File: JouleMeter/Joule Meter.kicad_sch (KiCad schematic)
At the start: 65 parts, among them J1 XT60-M, J2 XT60-M, J3 22035035, J4 22035035, U1 LMR36510, U3 INA240A1PW, U4 ADS1118IDGS-Q1, U5 MCP6286T-E/OT1

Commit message: Complete Draft Layout
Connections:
- net GND: now also U1.9 (PAD)
- net CAN_H renamed CAN_P
- net CAN_L renamed CAN_N
- no-connect marks 2 -> 1
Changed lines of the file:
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@@
+	)
+	(junction
+		(at 104.14 85.09)
+		(diameter 0)
+		(color 0 0 0 0)
 	)
 	(junction
@@
 		(at 229.87 146.05)
 	)
-	(no_connect
-		(at 106.68 83.82)
-	)
 	(wire
 		(pts
@@
 	(wire
 		(pts
+			(xy 106.68 85.09) (xy 104.14 85.09)
+		)
+		(stroke
+			(width 0)
+			(type default)
+		)
+	)
+	(wire
+		(pts
 			(xy 200.66 55.88) (xy 200.66 58.42)
 		)
@@
 	(wire
 		(pts
+			(xy 104.14 85.09) (xy 104.14 86.36)
+		)
+		(stroke
+			(width 0)
+			(type default)
+		)
+	)
+	(wire
+		(pts
 			(xy 196.85 143.51) (xy 196.85 146.05)
 		)
@@
 	(wire
 		(pts
-			(xy 104.14 83.82) (xy 104.14 86.36)
+			(xy 104.14 83.82) (xy 104.14 85.09)
 		)
 		(stroke
@@
 		(pts
 			(xy 304.8 71.12) (xy 304.8 76.2)
+		)
+		(stroke
+			(width 0)
+			(type default)
+		)
+	)
+	(wire
+		(pts
+			(xy 106.68 83.82) (xy 106.68 85.09)
 		)
 		(stroke
@@
 		)
 	)
-	(label "CAN_L"
+	(label "CAN_N"
 		(at 285.75 200.66 180)
 		(effects
@@
 		)
 	)
-	(label "CAN_H"
+	(label "CAN_P"
 		(at 280.67 185.42 180)
 		(effects

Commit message: PCB Complete Draft
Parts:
- removed TP19: CT-RXD, TestPoint:TestPoint_Pad_1.0x1.0mm, symbol Connector:TestPoint
- removed TP20: CT-TXD, TestPoint:TestPoint_Pad_1.0x1.0mm, symbol Connector:TestPoint
- added J5: M22-7130442, SMV_Joule:HARWIN_M22-7130442, symbol Joule Meter:M22-7130442
- R0: footprint SMV_Joule:WSBS8518_VIS-L -> SMV_Joule:RESC10052X145N
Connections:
- net CAN-TXD: now also J5.1
- net CAN_RXD: now also J5.4
- net GND: now also J5.2, J5.3
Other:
- moved on the sheet: C21, C23, J3, J4, MCP2562, TP15, TP16

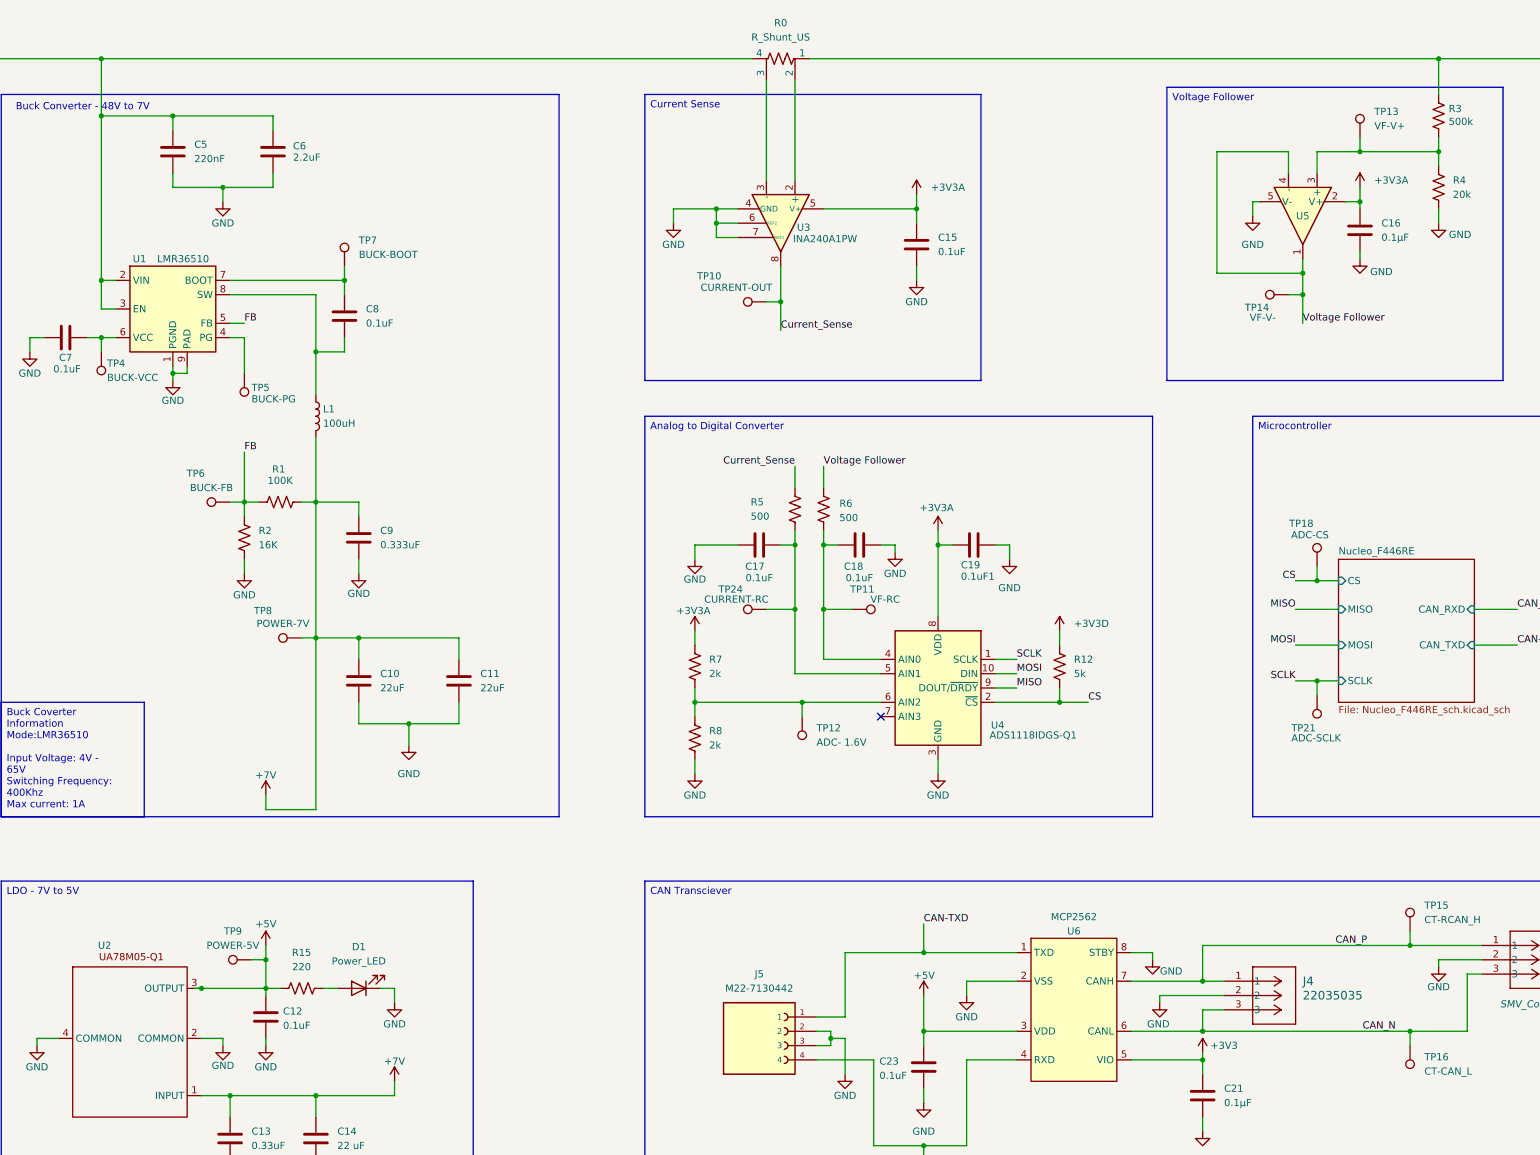
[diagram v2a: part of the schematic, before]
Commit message: Revised Version Part 1
Implemented changes from Google Docs and Dylan
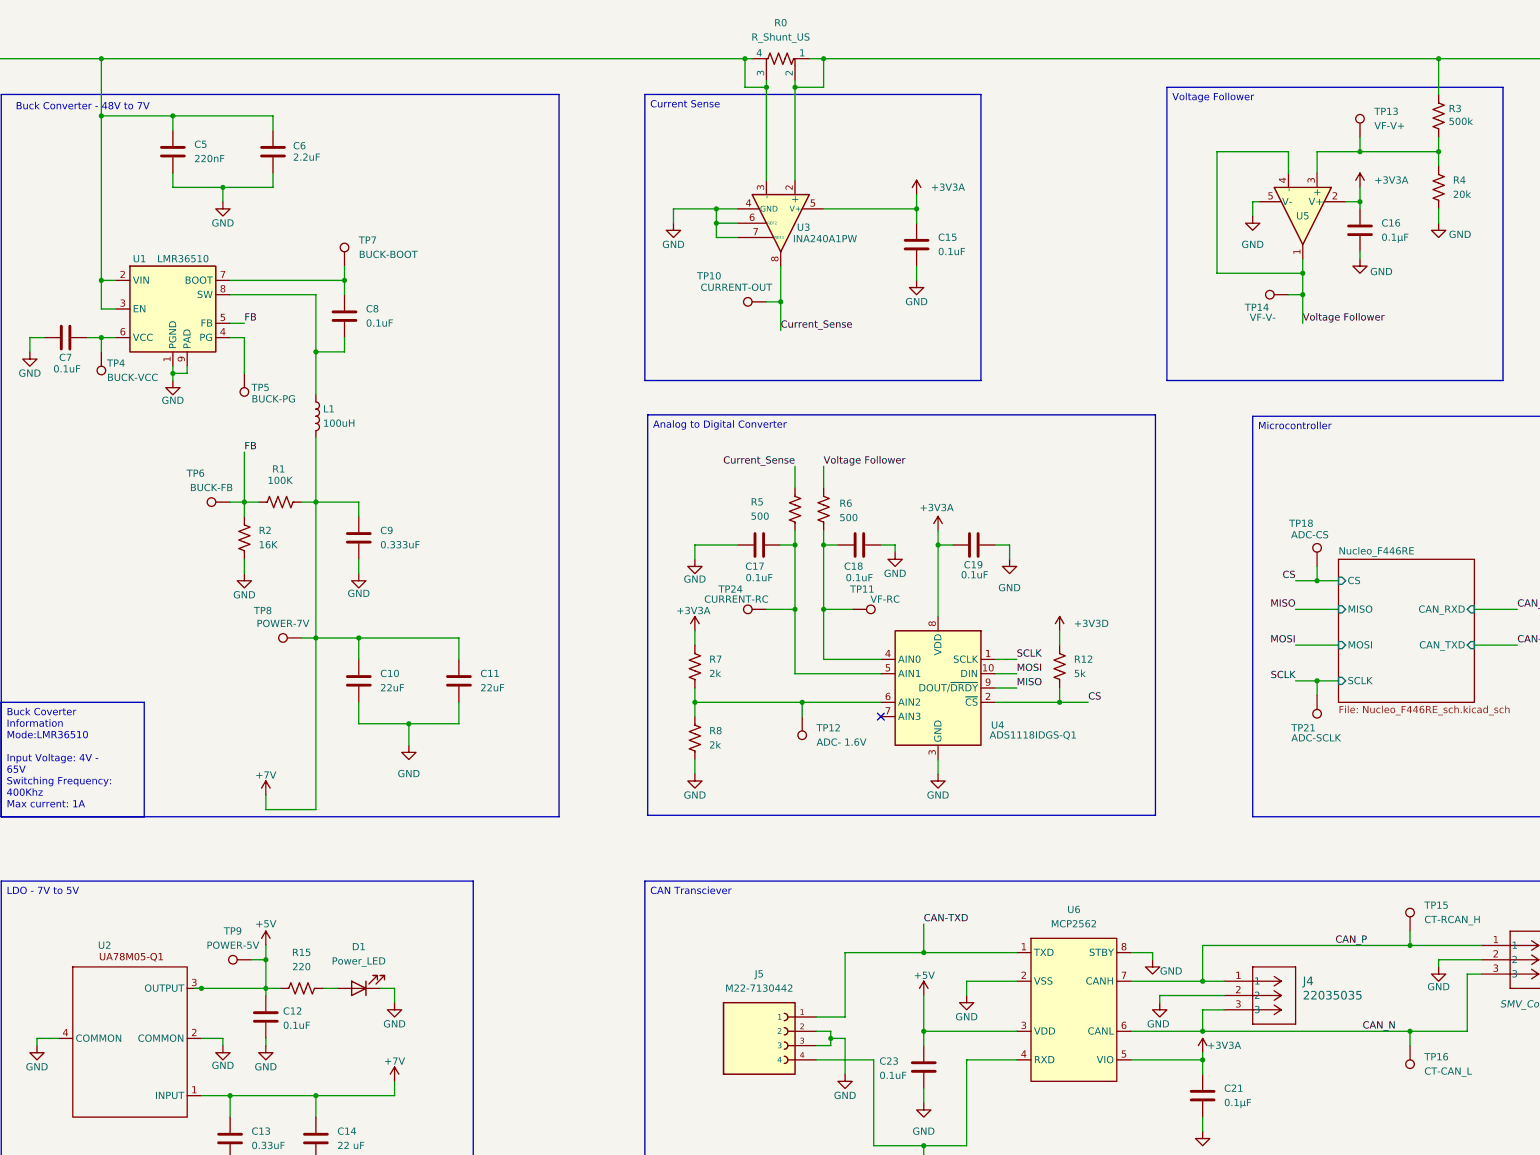
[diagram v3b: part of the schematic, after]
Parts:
- C19: renamed from 0.1uF1; value C19 -> 0.1uF
- U6: renamed from MCP2562; value U6 -> MCP2562
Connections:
- net +3V3 is gone; now on net +3V3A: C21.1, U6.5 (VIO)
- net at C1.2, C2.1, J1.P (POS)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: now also R0.2, U3.2 (+)
- net at R0.3, U3.3 (-): now also C3.2, C4.1, C5.2, C6.2, J2.P (POS), R0.4, TP3.1, U1.2 (VIN), U1.3 (EN)
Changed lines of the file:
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@@
 	(text_box "Analog to Digital Converter"
 		(exclude_from_sim no)
-		(at 187.96 92.71 0)
+		(at 188.468 92.456 0)
 		(size 90.17 71.12)
 		(margins 0.9525 0.9525 0.9525 0.9525)
@@
 	)
 	(junction
+		(at 209.55 34.29)
+		(diameter 0)
+		(color 0 0 0 0)
+	)
+	(junction
 		(at 328.93 45.72)
 		(diameter 0)
@@
 	)
 	(junction
+		(at 219.71 29.21)
+		(diameter 0)
+		(color 0 0 0 0)
+	)
+	(junction
 		(at 323.85 186.69)
 		(diameter 0)
@@
 	)
 	(junction
+		(at 214.63 34.29)
+		(diameter 0)
+		(color 0 0 0 0)
+	)
+	(junction
 		(at 129.54 107.95)
 		(diameter 0)
@@
 	)
 	(junction
+		(at 205.74 29.21)
+		(diameter 0)
+		(color 0 0 0 0)
+	)
+	(junction
 		(at 363.22 29.21)
 		(diameter 0)
@@
 	(wire
 		(pts
-			(xy 214.63 33.02) (xy 214.63 50.8)
+			(xy 214.63 33.02) (xy 214.63 34.29)
 		)
 		(stroke
@@
 	(wire
 		(pts
-			(xy 217.17 29.21) (xy 328.93 29.21)
+			(xy 217.17 29.21) (xy 219.71 29.21)
 		)
 		(stroke
@@
 	(wire
 		(pts
+			(xy 209.55 34.29) (xy 205.74 34.29)
+		)
+		(stroke
+			(width 0)
+			(type default)
+		)
+	)
+	(wire
+		(pts
 			(xy 196.85 115.57) (xy 204.47 115.57)
 		)
@@
 	(wire
 		(pts
+			(xy 205.74 34.29) (xy 205.74 29.21)
+		)
+		(stroke
+			(width 0)
+			(type default)
+		)
+	)
+	(wire
+		(pts
 			(xy 129.54 224.79) (xy 129.54 228.6)
 		)
@@
 	(wire
 		(pts
+			(xy 219.71 29.21) (xy 328.93 29.21)
+		)
+		(stroke
+			(width 0)
+			(type default)
+		)
+	)
+	(wire
+		(pts
 			(xy 287.02 201.93) (xy 323.85 201.93)
 		)
@@
 	(wire
 		(pts
+			(xy 214.63 34.29) (xy 214.63 50.8)
+		)
+		(stroke
+			(width 0)
+			(type default)
+		)
+	)
+	(wire
+		(pts
 			(xy 287.02 193.04) (xy 290.83 193.04)
 		)
@@
 	(wire
 		(pts
-			(xy 91.44 29.21) (xy 207.01 29.21)
+			(xy 91.44 29.21) (xy 205.74 29.21)
 		)
 		(stroke
@@
 	(wire
 		(pts
+			(xy 205.74 29.21) (xy 207.01 29.21)
+		)
+		(stroke
+			(width 0)
+			(type default)
+		)
+	)
+	(wire
+		(pts
 			(xy 137.16 147.32) (xy 146.05 147.32)
 		)
@@
 	(wire
 		(pts
+			(xy 214.63 34.29) (xy 219.71 34.29)
+		)
+		(stroke
+			(width 0)
+			(type default)
+		)
+	)
+	(wire
+		(pts
 			(xy 118.11 189.23) (xy 120.65 189.23)
 		)
@@
 	(wire
 		(pts
-			(xy 209.55 33.02) (xy 209.55 50.8)
+			(xy 209.55 33.02) (xy 209.55 34.29)
 		)
 		(stroke
@@
 	(wire
 		(pts
+			(xy 219.71 34.29) (xy 219.71 29.21)
+		)
+		(stroke
+			(width 0)
+			(type default)
+		)
+	)
+	(wire
+		(pts
 			(xy 116.84 107.95) (xy 119.38 107.95)
 		)
@@
 	(wire
 		(pts
+			(xy 209.55 34.29) (xy 209.55 50.8)
+		)
+		(stroke
+			(width 0)
+			(type default)
+		)
+	)
+	(wire
+		(pts
 			(xy 120.65 189.23) (xy 120.65 194.31)
 		)
@@
 			)
 		)
-		(property "Value" "+3V3"
+		(property "Value" "+3V3A"
 			(at 290.83 204.47 0)
 			(effects
@@
 		(on_board yes)
 		(dnp no)
-		(property "Reference" "0.1uF1"
-			(at 244.094 121.158 90)
+		(property "Reference" "C19"
+			(at 244.602 119.126 90)
 			(effects
 				(font
@@
 			)
 		)
-		(property "Value" "C19"
-			(at 244.094 119.126 90)
+		(property "Value" "0.1uF"
+			(at 244.094 120.904 90)
 			(effects
 				(font
@@
 			(project "Joule Meter"
 				(path "/3c05686f-5554-4d70-b348-db94545e7981"
-					(reference "0.1uF1")
+					(reference "C19")
 					(unit 1)
 				)
@@
 		(dnp no)
 		(fields_autoplaced yes)
-		(property "Reference" "MCP2562"
-			(at 264.16 181.61 0)
+		(property "Reference" "U6"
+			(at 264.16 180.34 0)
 			(effects
 				(font
@@
 			)
 		)
-		(property "Value" "U6"
-			(at 264.16 184.15 0)
+		(property "Value" "MCP2562"
+			(at 264.16 182.88 0)
 			(effects
 				(font
@@
 			(project ""
 				(path "/3c05686f-5554-4d70-b348-db94545e7981"
-					(reference "MCP2562")
+					(reference "U6")
 					(unit 1)
 				)

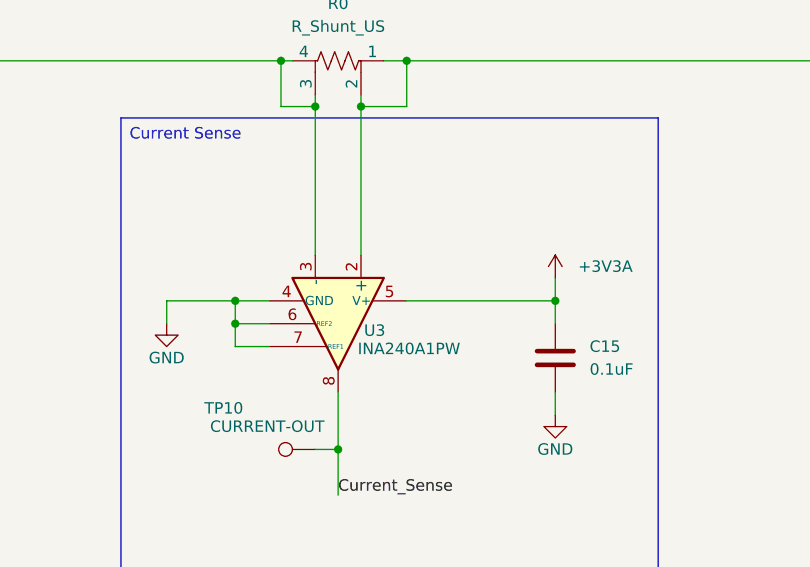
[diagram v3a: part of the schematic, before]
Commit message: Verification Changes (No Peninsula Fixes)
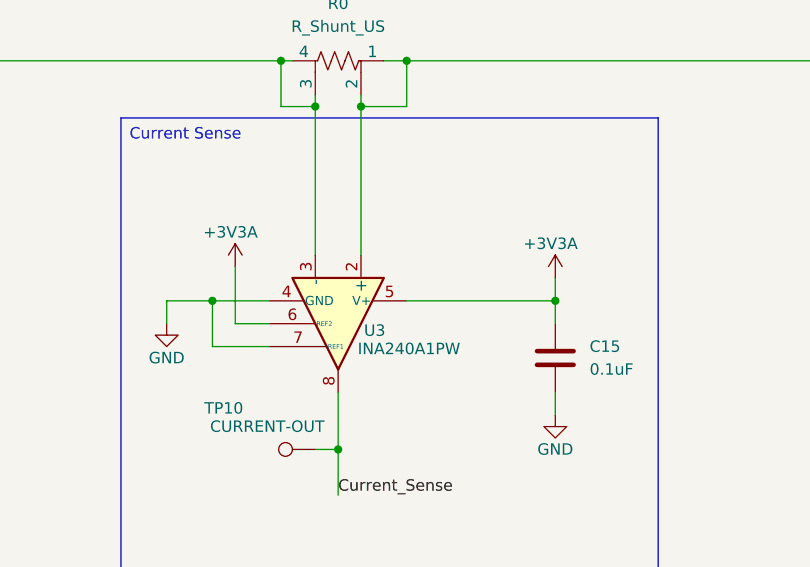
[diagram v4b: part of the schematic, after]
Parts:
- U6: footprint SMV_Joule:PDIP8_300MC_MCH -> SMV_Joule:SOIC8-N_MC_MCH-M
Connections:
- net +3V3A: now also U3.6 (REF2)
- net GND: no longer U3.6 (REF2)
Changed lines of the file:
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@@
 	)
 	(junction
+		(at 198.12 55.88)
+		(diameter 0)
+		(color 0 0 0 0)
+	)
+	(junction
 		(at 287.02 193.04)
 		(diameter 0)
@@
 	)
 	(junction
-		(at 200.66 55.88)
-		(diameter 0)
-		(color 0 0 0 0)
-	)
-	(junction
 		(at 261.62 143.51)
 		(diameter 0)
@@
 		(color 0 0 0 0)
 	)
-	(junction
-		(at 200.66 58.42)
-		(diameter 0)
-		(color 0 0 0 0)
-	)
 	(no_connect
 		(at 229.87 146.05)
@@
 	(wire
 		(pts
+			(xy 200.66 52.07) (xy 200.66 58.42)
+		)
+		(stroke
+			(width 0)
+			(type default)
+		)
+	)
+	(wire
+		(pts
 			(xy 381 41.91) (xy 381 45.72)
 		)
@@
 	(wire
 		(pts
-			(xy 200.66 60.96) (xy 204.47 60.96)
+			(xy 220.98 201.93) (xy 220.98 203.2)
 		)
 		(stroke
@@
 	(wire
 		(pts
-			(xy 220.98 201.93) (xy 220.98 203.2)
+			(xy 198.12 60.96) (xy 204.47 60.96)
 		)
 		(stroke
@@
 	(wire
 		(pts
+			(xy 198.12 55.88) (xy 204.47 55.88)
+		)
+		(stroke
+			(width 0)
+			(type default)
+		)
+	)
+	(wire
+		(pts
 			(xy 205.74 34.29) (xy 205.74 29.21)
 		)
@@
 	(wire
 		(pts
-			(xy 200.66 55.88) (xy 200.66 58.42)
-		)
-		(stroke
-			(width 0)
-			(type default)
-		)
-	)
-	(wire
-		(pts
 			(xy 237.49 212.09) (xy 237.49 214.63)
 		)
@@
 	(wire
 		(pts
+			(xy 198.12 60.96) (xy 198.12 55.88)
+		)
+		(stroke
+			(width 0)
+			(type default)
+		)
+	)
+	(wire
+		(pts
 			(xy 381 29.21) (xy 393.7 29.21)
 		)
@@
 	(wire
 		(pts
-			(xy 193.04 55.88) (xy 200.66 55.88)
-		)
-		(stroke
-			(width 0)
-			(type default)
-		)
-	)
-	(wire
-		(pts
 			(xy 335.28 127) (xy 342.9 127)
 		)
@@
 	(wire
 		(pts
-			(xy 200.66 55.88) (xy 204.47 55.88)
+			(xy 193.04 55.88) (xy 198.12 55.88)
 		)
 		(stroke
@@
 	(wire
 		(pts
-			(xy 200.66 58.42) (xy 200.66 60.96)
-		)
-		(stroke
-			(width 0)
-			(type default)
-		)
-	)
-	(wire
-		(pts
 			(xy 323.85 201.93) (xy 334.01 201.93)
 		)
@@
 		(on_board yes)
 		(dnp no)
-		(fields_autoplaced yes)
 		(property "Reference" "#PWR01"
 			(at 236.22 57.15 0)
@@
 		)
 		(property "Value" "+3V3A"
-			(at 238.76 52.0699 0)
+			(at 232.664 49.53 0)
 			(effects
 				(font
@@
 	)
 	(symbol
+		(lib_id "power:+3V3")
+		(at 200.66 52.07 0)
+		(unit 1)
+		(exclude_from_sim no)
+		(in_bom yes)
+		(on_board yes)
+		(dnp no)
+		(property "Reference" "#PWR026"
+			(at 200.66 55.88 0)
+			(effects
+				(font
+					(size 1.27 1.27)
+				)
+				(hide yes)
+			)
+		)
+		(property "Value" "+3V3A"
+			(at 197.104 48.26 0)
+			(effects
+				(font
+					(size 1.27 1.27)
+				)
+				(justify left)
+			)
+		)
+		(property "Footprint" ""
+			(at 200.66 52.07 0)
+			(effects
+				(font
+					(size 1.27 1.27)
+				)
+				(hide yes)
+			)
+		)
+		(property "Datasheet" ""
+			(at 200.66 52.07 0)
+			(effects
+				(font
+					(size 1.27 1.27)
+				)
+				(hide yes)
+			)
+		)
+		(property "Description" "Power symbol creates a global label with name \"+3V3\""
+			(at 200.66 52.07 0)
+			(effects
+				(font
+					(size 1.27 1.27)
+				)
+				(hide yes)
+			)
+		)
+		(pin "1"
+		)
+		(instances
+			(project "Joule Meter"
+				(path "/3c05686f-5554-4d70-b348-db94545e7981"
+					(reference "#PWR026")
+					(unit 1)
+				)
+			)
+		)
+	)
+	(symbol
 		(lib_id "Device:C")
 		(at 226.06 115.57 270)
@@
 			)
 		)
-		(property "Footprint" "SMV_Joule:PDIP8_300MC_MCH"
+		(property "Footprint" "SMV_Joule:SOIC8-N_MC_MCH-M"
 			(at 264.16 198.12 0)
 			(effects

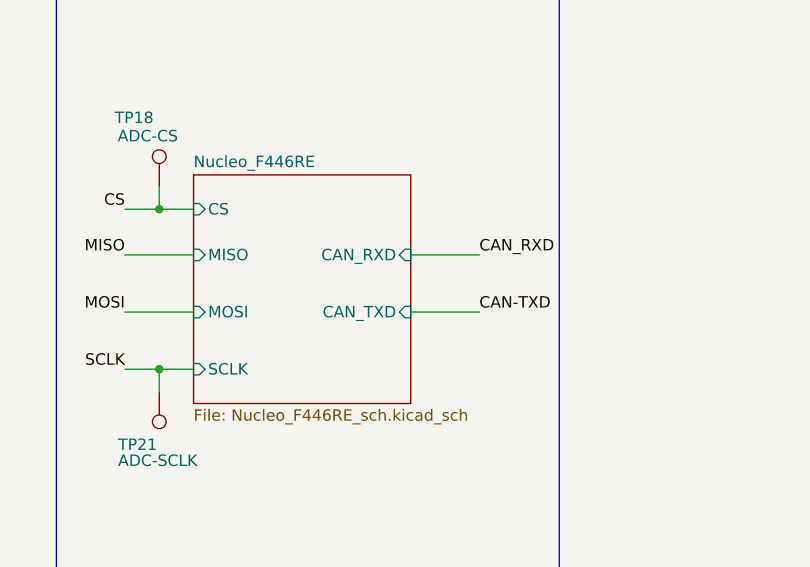
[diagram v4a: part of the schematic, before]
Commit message: Joule Meter Final
-Removed Pinnulas
-Added specific capacitor links for capacitors with a 48V across.
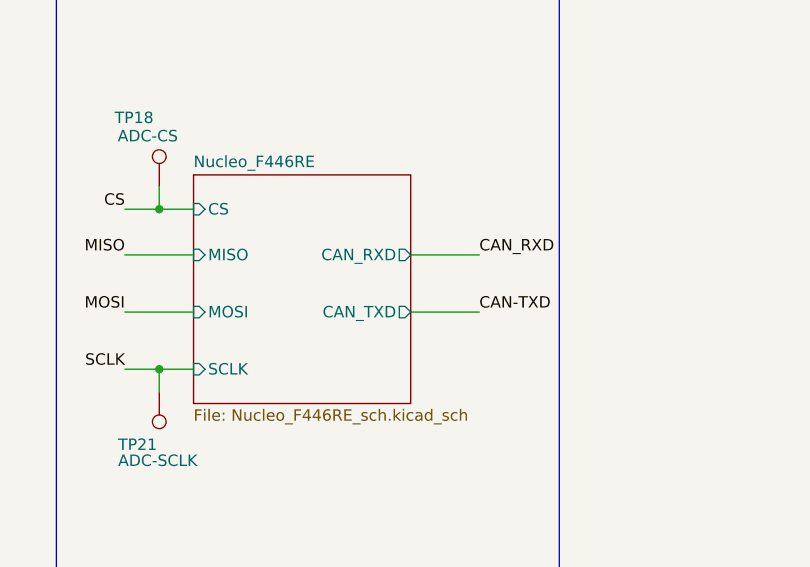
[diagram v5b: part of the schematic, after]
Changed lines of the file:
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@@
 		(title "Joule Meter (w/ Current Sense)")
 		(date "9/16/2025")
-		(rev "10/17/2025")
+		(rev "12/26/2025")
 		(company "by Sergio Gonzalez")
 		(comment 1 "University of California, Los Angeles")
@@
 			)
 		)
-		(property "Datasheet" "~"
+		(property "Datasheet" "https://www.digikey.com/en/products/detail/nextgen-components/0805B225K500CC/18677030"
 			(at 121.92 45.72 0)
 			(effects
@@
 			)
 		)
-		(property "Datasheet" "~"
+		(property "Datasheet" "https://www.digikey.com/en/products/detail/nextgen-components/0805W106K500CC/18677029"
 			(at 63.5 38.1 0)
 			(effects
@@
 			)
 		)
-		(property "Datasheet" "~"
+		(property "Datasheet" "https://www.digikey.com/en/products/detail/nextgen-components/0805B224K101CC/18668218"
 			(at 104.14 45.72 0)
 			(effects
@@
 			)
 		)
-		(property "Datasheet" "~"
+		(property "Datasheet" "https://www.digikey.com/en/products/detail/nextgen-components/0805W106K500CC/18677029"
 			(at 381 38.1 0)
 			(effects
@@
 			)
 		)
-		(pin "CAN_RXD" input
+		(pin "CAN_RXD" output
 			(at 335.28 127 0)
 			(effects
@@
 			)
 		)
-		(pin "CAN_TXD" input
+		(pin "CAN_TXD" output
 			(at 335.28 133.35 0)
 			(effects

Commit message: changed the inductor footprint
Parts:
- L1: footprint Inductor_SMD:L_1206_3216Metric_Pad1.22x1.90mm_HandSolder -> Personal:IND_BOURNS_SRN8040
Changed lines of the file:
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@@
 			)
 		)
-		(property "Footprint" "Inductor_SMD:L_1206_3216Metric_Pad1.22x1.90mm_HandSolder"
+		(property "Footprint" "Personal:IND_BOURNS_SRN8040"
 			(at 129.54 92.71 0)
 			(effects

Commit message: added two new caps next to ferrite bead
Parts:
- U2: value ~ -> (none)
